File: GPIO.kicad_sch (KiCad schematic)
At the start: 18 parts, among them U1 74LS245

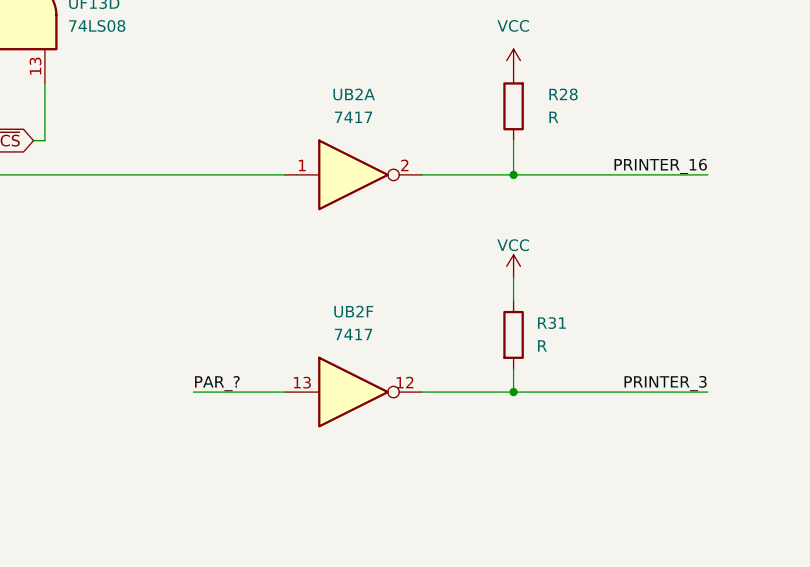
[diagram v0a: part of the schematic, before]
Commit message: Graphical error: 7417 is a non-inverting buffer
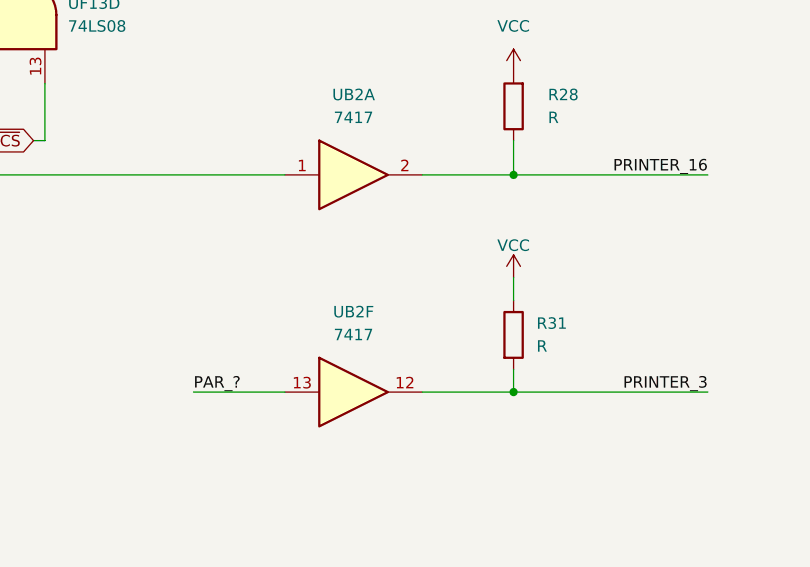
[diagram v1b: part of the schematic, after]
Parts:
- UB2: symbol 74xx:74LS04 -> 74xx:74LS07
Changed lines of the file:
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@@
     )
   )
-  (symbol (lib_id "74xx:74LS04") (at 198.12 151.13 0) (unit 6)
+  (symbol (lib_id "74xx:74LS07") (at 198.12 151.13 0) (unit 6)
     (in_bom yes) (on_board yes) (dnp no) (fields_autoplaced)
     (property "Reference" "UB2" (at 198.12 142.24 0)
@@
       (effects (font (size 1.27 1.27)) hide)
     )
-    (property "Datasheet" "http://www.ti.com/lit/gpn/sn74LS04" (at 198.12 151.13 0)
+    (property "Datasheet" "www.ti.com/lit/ds/symlink/sn74ls07.pdf" (at 198.12 151.13 0)
       (effects (font (size 1.27 1.27)) hide)
     )
@@
     )
   )
-  (symbol (lib_id "74xx:74LS04") (at 198.12 127 0) (unit 1)
+  (symbol (lib_id "74xx:74LS07") (at 198.12 127 0) (unit 1)
     (in_bom yes) (on_board yes) (dnp no) (fields_autoplaced)
     (property "Reference" "UB2" (at 198.12 118.11 0)
@@
       (effects (font (size 1.27 1.27)) hide)
     )
-    (property "Datasheet" "http://www.ti.com/lit/gpn/sn74LS04" (at 198.12 127 0)
+    (property "Datasheet" "www.ti.com/lit/ds/symlink/sn74ls07.pdf" (at 198.12 127 0)
       (effects (font (size 1.27 1.27)) hide)
     )

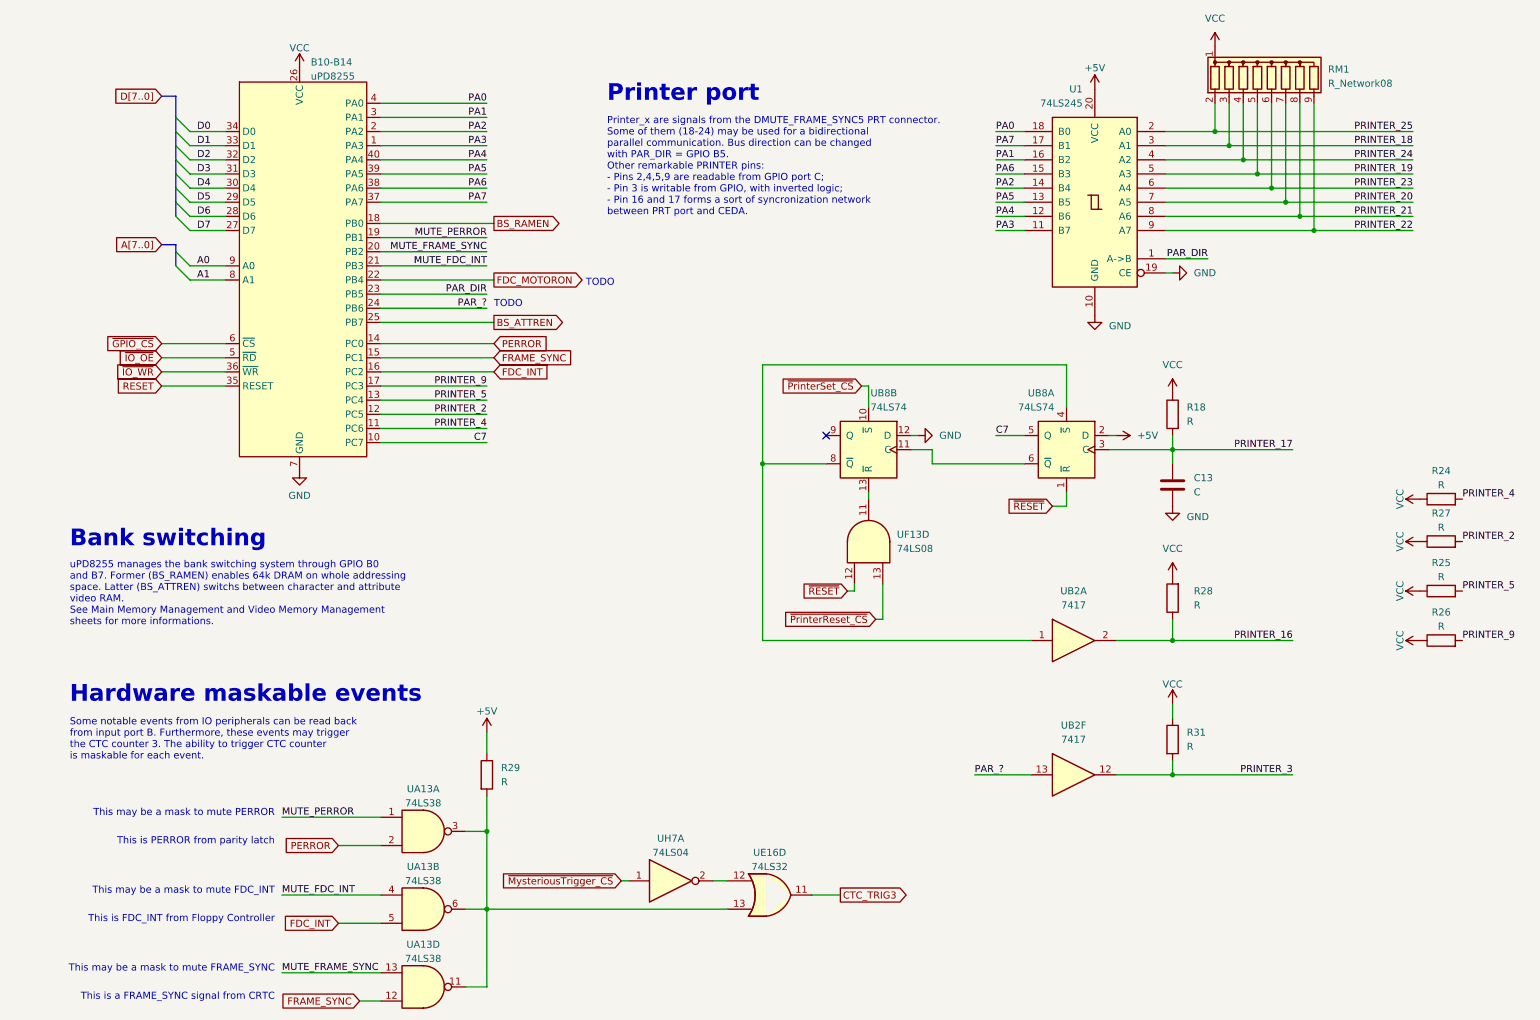
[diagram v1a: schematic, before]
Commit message: Components renaming according to the Uxy convention.
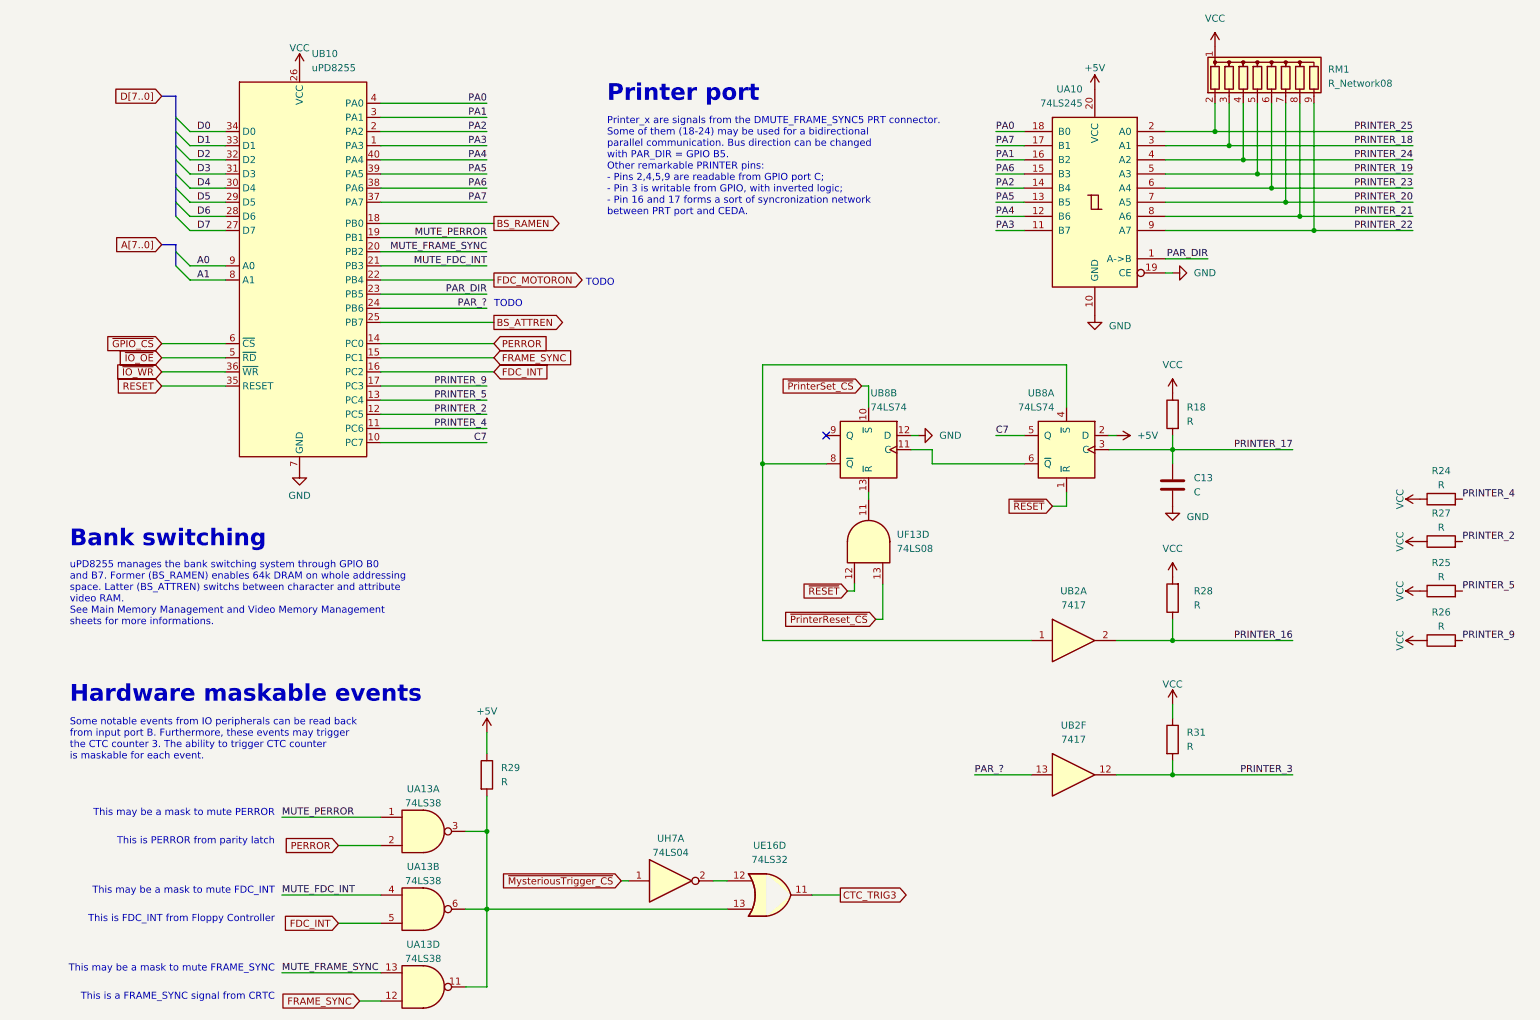
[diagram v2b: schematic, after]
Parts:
- renumbered U1 to UA10, B10-B14 to UB10
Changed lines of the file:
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@@
   (symbol (lib_id "74xx:74LS32") (at 143.51 172.72 0) (unit 4)
     (in_bom yes) (on_board yes) (dnp no) (fields_autoplaced)
-    (property "Reference" "UE16" (at 143.51 165.1 0)
-      (effects (font (size 1.27 1.27)))
-    )
-    (property "Value" "74LS32" (at 143.51 167.64 0)
+    (property "Reference" "UE16" (at 143.51 163.83 0)
+      (effects (font (size 1.27 1.27)))
+    )
+    (property "Value" "74LS32" (at 143.51 166.37 0)
       (effects (font (size 1.27 1.27)))
     )
@@
   (symbol (lib_id "ceda:uPD8255") (at 59.055 59.69 0) (unit 1)
     (in_bom yes) (on_board yes) (dnp no) (fields_autoplaced)
-    (property "Reference" "B10-B14" (at 61.0744 23.0972 0)
-      (effects (font (size 1.27 1.27)) (justify left))
-    )
-    (property "Value" "uPD8255" (at 61.0744 25.6341 0)
+    (property "Reference" "UB10" (at 61.2491 21.59 0)
+      (effects (font (size 1.27 1.27)) (justify left))
+    )
+    (property "Value" "uPD8255" (at 61.2491 24.13 0)
       (effects (font (size 1.27 1.27)) (justify left))
     )
@@
       (project "ceda"
         (path "/12a6dbe3-008d-4c5b-88f6-9f1c816060be/23c42ab9-740a-4e84-88f1-9f74965e7273"
-          (reference "B10-B14") (unit 1)
+          (reference "UB10") (unit 1)
         )
       )
@@
   (symbol (lib_id "74xx:74LS245") (at 201.93 48.26 0) (mirror y) (unit 1)
     (in_bom yes) (on_board yes) (dnp no)
-    (property "Reference" "U1" (at 199.7359 27.94 0)
+    (property "Reference" "UA10" (at 199.7359 27.94 0)
       (effects (font (size 1.27 1.27)) (justify left))
     )
@@
       (project "ceda"
         (path "/12a6dbe3-008d-4c5b-88f6-9f1c816060be/23c42ab9-740a-4e84-88f1-9f74965e7273"
-          (reference "U1") (unit 1)
-        )
-      )
+          (reference "UA10") (unit 1)
+        )
+      )

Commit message: VCC -> +5V
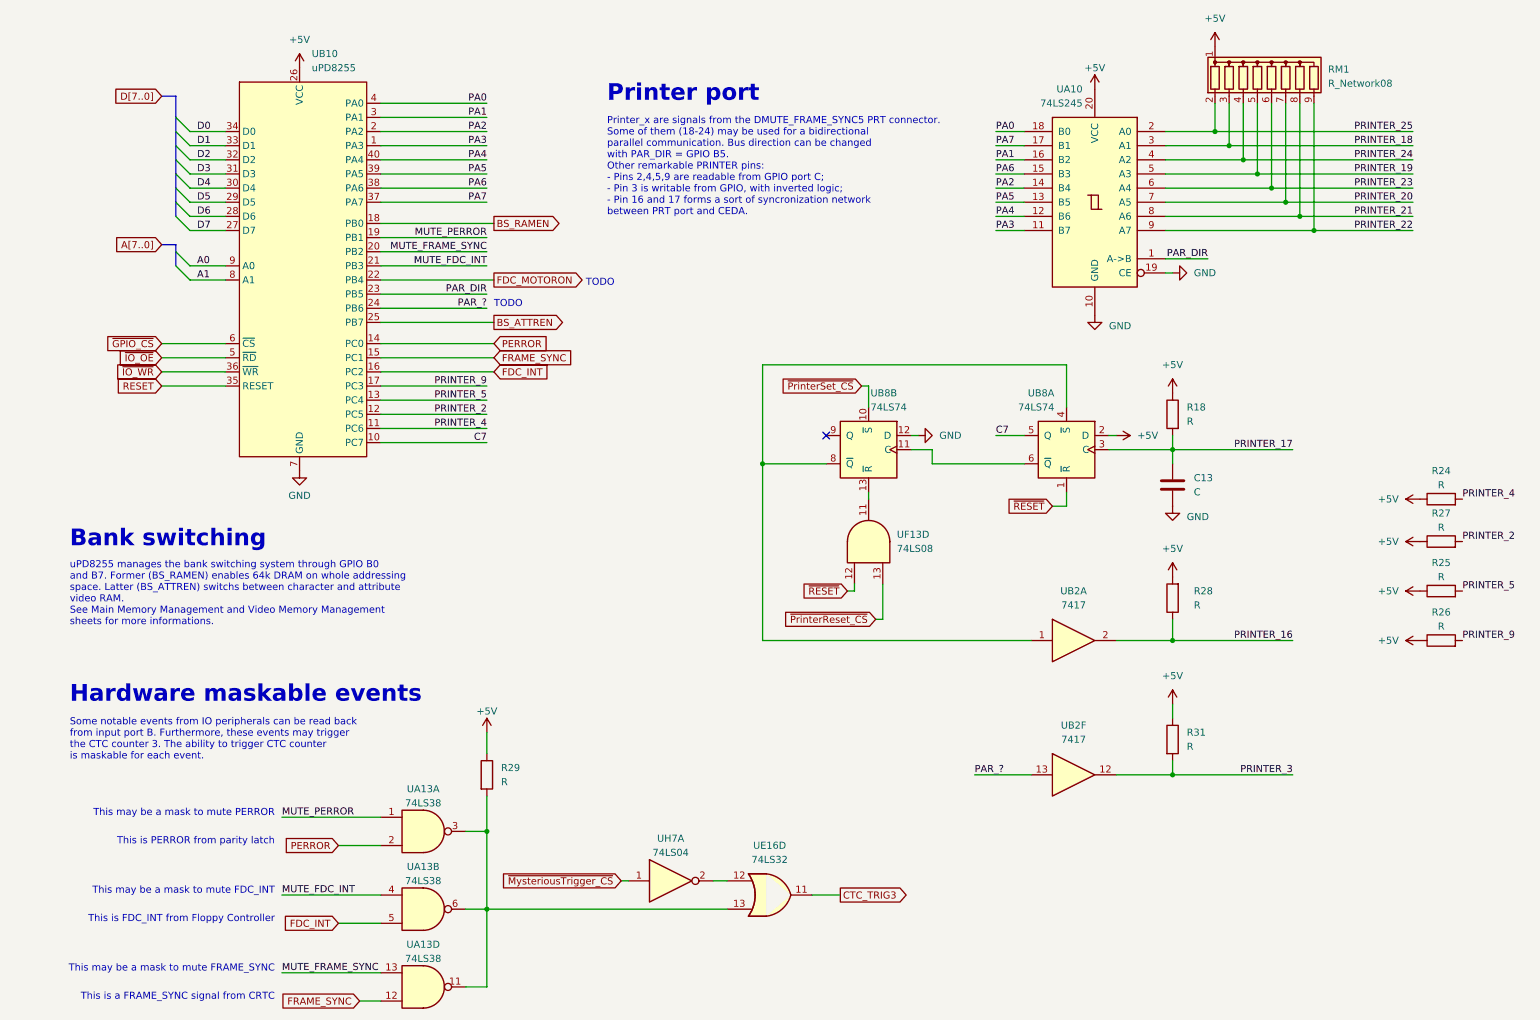
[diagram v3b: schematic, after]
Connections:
- net VCC is gone; now on net +5V: R18.1, R24.1, R25.1, R26.1, R27.1, R28.2, R31.1, RM1.1 (common), UB10.26 (VCC)
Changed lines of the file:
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@@
     )
   )
-  (symbol (lib_id "power:VCC") (at 260.35 109.22 90) (unit 1)
-    (in_bom yes) (on_board yes) (dnp no) (fields_autoplaced)
-    (property "Reference" "#PWR099" (at 264.16 109.22 0)
-      (effects (font (size 1.27 1.27)) hide)
-    )
-    (property "Value" "VCC" (at 256.7742 109.22 0)
-      (effects (font (size 1.27 1.27)))
+  (symbol (lib_id "power:+5V") (at 260.35 109.22 90) (unit 1)
+    (in_bom yes) (on_board yes) (dnp no) (fields_autoplaced)
+    (property "Reference" "#PWR?" (at 264.16 109.22 0)
+      (effects (font (size 1.27 1.27)) hide)
+    )
+    (property "Value" "+5V" (at 256.54 109.22 90)
+      (effects (font (size 1.27 1.27)) (justify left))
     )
     (property "Footprint" "" (at 260.35 109.22 0)
@@
       (project "ceda"
         (path "/12a6dbe3-008d-4c5b-88f6-9f1c816060be/23c42ab9-740a-4e84-88f1-9f74965e7273"
-          (reference "#PWR099") (unit 1)
+          (reference "#PWR?") (unit 1)
         )
       )
@@
     )
   )
-  (symbol (lib_id "power:VCC") (at 260.35 118.11 90) (unit 1)
-    (in_bom yes) (on_board yes) (dnp no) (fields_autoplaced)
-    (property "Reference" "#PWR0102" (at 264.16 118.11 0)
-      (effects (font (size 1.27 1.27)) hide)
-    )
-    (property "Value" "VCC" (at 256.7742 118.11 0)
-      (effects (font (size 1.27 1.27)))
+  (symbol (lib_id "power:+5V") (at 260.35 118.11 90) (unit 1)
+    (in_bom yes) (on_board yes) (dnp no) (fields_autoplaced)
+    (property "Reference" "#PWR?" (at 264.16 118.11 0)
+      (effects (font (size 1.27 1.27)) hide)
+    )
+    (property "Value" "+5V" (at 256.54 118.11 90)
+      (effects (font (size 1.27 1.27)) (justify left))
     )
     (property "Footprint" "" (at 260.35 118.11 0)
@@
       (project "ceda"
         (path "/12a6dbe3-008d-4c5b-88f6-9f1c816060be/23c42ab9-740a-4e84-88f1-9f74965e7273"
-          (reference "#PWR0102") (unit 1)
+          (reference "#PWR?") (unit 1)
         )
       )
@@
     )
   )
-  (symbol (lib_id "power:VCC") (at 223.52 20.32 0) (mirror y) (unit 1)
-    (in_bom yes) (on_board yes) (dnp no) (fields_autoplaced)
-    (property "Reference" "#PWR038" (at 223.52 24.13 0)
-      (effects (font (size 1.27 1.27)) hide)
-    )
-    (property "Value" "VCC" (at 223.52 15.24 0)
+  (symbol (lib_id "power:+5V") (at 223.52 20.32 0) (mirror y) (unit 1)
+    (in_bom yes) (on_board yes) (dnp no) (fields_autoplaced)
+    (property "Reference" "#PWR?" (at 223.52 24.13 0)
+      (effects (font (size 1.27 1.27)) hide)
+    )
+    (property "Value" "+5V" (at 223.52 15.24 0)
       (effects (font (size 1.27 1.27)))
     )
@@
       (project "ceda"
         (path "/12a6dbe3-008d-4c5b-88f6-9f1c816060be/23c42ab9-740a-4e84-88f1-9f74965e7273"
-          (reference "#PWR038") (unit 1)
+          (reference "#PWR?") (unit 1)
         )
       )
@@
     )
   )
-  (symbol (lib_id "power:VCC") (at 215.9 138.43 0) (unit 1)
-    (in_bom yes) (on_board yes) (dnp no) (fields_autoplaced)
-    (property "Reference" "#PWR098" (at 215.9 142.24 0)
-      (effects (font (size 1.27 1.27)) hide)
-    )
-    (property "Value" "VCC" (at 215.9 134.8542 0)
+  (symbol (lib_id "power:+5V") (at 215.9 138.43 0) (unit 1)
+    (in_bom yes) (on_board yes) (dnp no) (fields_autoplaced)
+    (property "Reference" "#PWR?" (at 215.9 142.24 0)
+      (effects (font (size 1.27 1.27)) hide)
+    )
+    (property "Value" "+5V" (at 215.9 133.35 0)
       (effects (font (size 1.27 1.27)))
     )
@@
       (project "ceda"
         (path "/12a6dbe3-008d-4c5b-88f6-9f1c816060be/23c42ab9-740a-4e84-88f1-9f74965e7273"
-          (reference "#PWR098") (unit 1)
+          (reference "#PWR?") (unit 1)
         )
       )
@@
     )
   )
-  (symbol (lib_id "power:VCC") (at 215.9 115.57 0) (unit 1)
-    (in_bom yes) (on_board yes) (dnp no) (fields_autoplaced)
-    (property "Reference" "#PWR0103" (at 215.9 119.38 0)
-      (effects (font (size 1.27 1.27)) hide)
-    )
-    (property "Value" "VCC" (at 215.9 110.49 0)
+  (symbol (lib_id "power:+5V") (at 215.9 115.57 0) (unit 1)
+    (in_bom yes) (on_board yes) (dnp no) (fields_autoplaced)
+    (property "Reference" "#PWR?" (at 215.9 119.38 0)
+      (effects (font (size 1.27 1.27)) hide)
+    )
+    (property "Value" "+5V" (at 215.9 110.49 0)
       (effects (font (size 1.27 1.27)))
     )
@@
       (project "ceda"
         (path "/12a6dbe3-008d-4c5b-88f6-9f1c816060be/23c42ab9-740a-4e84-88f1-9f74965e7273"
-          (reference "#PWR0103") (unit 1)
-        )
-      )
-    )
-  )
-  (symbol (lib_id "power:VCC") (at 215.9 82.55 0) (mirror y) (unit 1)
-    (in_bom yes) (on_board yes) (dnp no) (fields_autoplaced)
-    (property "Reference" "#PWR0105" (at 215.9 86.36 0)
-      (effects (font (size 1.27 1.27)) hide)
-    )
-    (property "Value" "VCC" (at 215.9 77.47 0)
+          (reference "#PWR?") (unit 1)
+        )
+      )
+    )
+  )
+  (symbol (lib_id "power:+5V") (at 215.9 82.55 0) (mirror y) (unit 1)
+    (in_bom yes) (on_board yes) (dnp no) (fields_autoplaced)
+    (property "Reference" "#PWR?" (at 215.9 86.36 0)
+      (effects (font (size 1.27 1.27)) hide)
+    )
+    (property "Value" "+5V" (at 215.9 77.47 0)
       (effects (font (size 1.27 1.27)))
     )
@@
       (project "ceda"
         (path "/12a6dbe3-008d-4c5b-88f6-9f1c816060be/23c42ab9-740a-4e84-88f1-9f74965e7273"
-          (reference "#PWR0105") (unit 1)
+          (reference "#PWR?") (unit 1)
         )
       )
@@
     )
   )
-  (symbol (lib_id "power:VCC") (at 59.055 24.13 0) (unit 1)
-    (in_bom yes) (on_board yes) (dnp no) (fields_autoplaced)
-    (property "Reference" "#PWR0175" (at 59.055 27.94 0)
-      (effects (font (size 1.27 1.27)) hide)
-    )
-    (property "Value" "VCC" (at 59.055 20.5542 0)
+  (symbol (lib_id "power:+5V") (at 59.055 24.13 0) (unit 1)
+    (in_bom yes) (on_board yes) (dnp no) (fields_autoplaced)
+    (property "Reference" "#PWR?" (at 59.055 27.94 0)
+      (effects (font (size 1.27 1.27)) hide)
+    )
+    (property "Value" "+5V" (at 59.055 19.05 0)
       (effects (font (size 1.27 1.27)))
     )
@@
       (project "ceda"
         (path "/12a6dbe3-008d-4c5b-88f6-9f1c816060be/23c42ab9-740a-4e84-88f1-9f74965e7273"
-          (reference "#PWR0175") (unit 1)
+          (reference "#PWR?") (unit 1)
         )
       )
@@
     )
   )
-  (symbol (lib_id "power:VCC") (at 260.35 101.6 90) (unit 1)
-    (in_bom yes) (on_board yes) (dnp no) (fields_autoplaced)
-    (property "Reference" "#PWR0100" (at 264.16 101.6 0)
-      (effects (font (size 1.27 1.27)) hide)
-    )
-    (property "Value" "VCC" (at 256.7742 101.6 0)
-      (effects (font (size 1.27 1.27)))
+  (symbol (lib_id "power:+5V") (at 260.35 101.6 90) (unit 1)
+    (in_bom yes) (on_board yes) (dnp no) (fields_autoplaced)
+    (property "Reference" "#PWR?" (at 264.16 101.6 0)
+      (effects (font (size 1.27 1.27)) hide)
+    )
+    (property "Value" "+5V" (at 256.54 101.6 90)
+      (effects (font (size 1.27 1.27)) (justify left))
     )
     (property "Footprint" "" (at 260.35 101.6 0)
@@
       (project "ceda"
         (path "/12a6dbe3-008d-4c5b-88f6-9f1c816060be/23c42ab9-740a-4e84-88f1-9f74965e7273"
-          (reference "#PWR0100") (unit 1)
+          (reference "#PWR?") (unit 1)
         )
       )
@@
     )
   )
-  (symbol (lib_id "power:VCC") (at 260.35 127 90) (unit 1)
-    (in_bom yes) (on_board yes) (dnp no) (fields_autoplaced)
-    (property "Reference" "#PWR0101" (at 264.16 127 0)
-      (effects (font (size 1.27 1.27)) hide)
-    )
-    (property "Value" "VCC" (at 256.7742 127 0)
-      (effects (font (size 1.27 1.27)))
+  (symbol (lib_id "power:+5V") (at 260.35 127 90) (unit 1)
+    (in_bom yes) (on_board yes) (dnp no) (fields_autoplaced)
+    (property "Reference" "#PWR?" (at 264.16 127 0)
+      (effects (font (size 1.27 1.27)) hide)
+    )
+    (property "Value" "+5V" (at 256.54 127 90)
+      (effects (font (size 1.27 1.27)) (justify left))
     )
     (property "Footprint" "" (at 260.35 127 0)
@@
       (project "ceda"
         (path "/12a6dbe3-008d-4c5b-88f6-9f1c816060be/23c42ab9-740a-4e84-88f1-9f74965e7273"
-          (reference "#PWR0101") (unit 1)
-        )
-      )
+          (reference "#PWR?") (unit 1)
+        )
+      )
